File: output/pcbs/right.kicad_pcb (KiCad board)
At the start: 2 copper layers, 137 x 129 mm, 79 parts

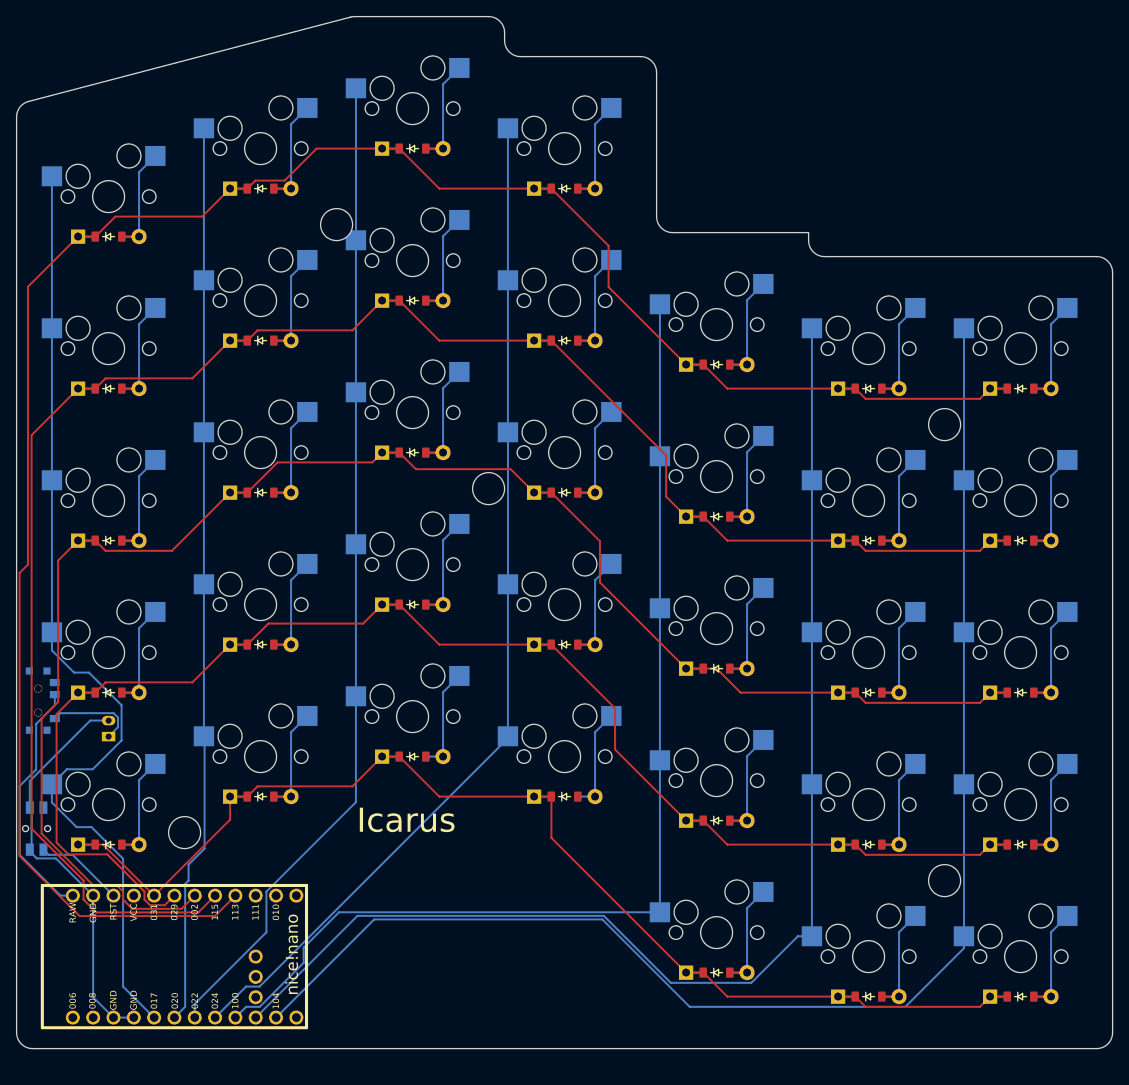
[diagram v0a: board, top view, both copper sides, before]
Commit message: redesign for short board, left but no right pcb. Final pcbs for old design
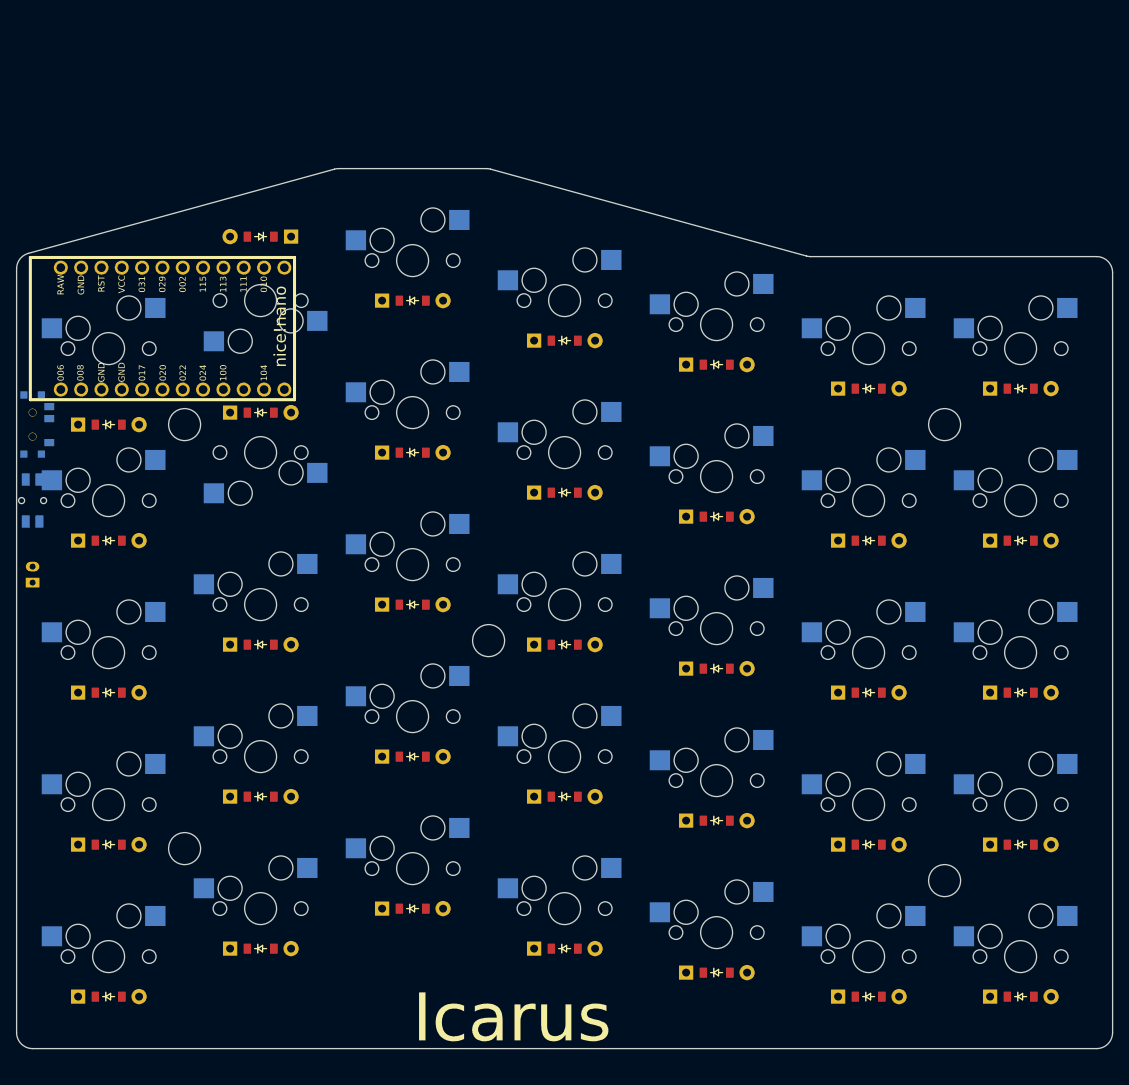
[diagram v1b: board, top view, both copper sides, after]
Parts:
- removed the ? at (261.5, 184.5)
- removed the ? at (299.5, 141.5)
- removed the ? at (280.5, 108.5)
- added ?: , HOLE_M2_TH, F.Cu at (299.5, 160.5)
- added ?: , HOLE_M2_TH, F.Cu at (261.5, 133.5)
- added ?: , HOLE_M2_TH, F.Cu at (261.5, 186.5)
- moved D29 84.2 mm to (252.0, 205.0)
- moved D30 84.2 mm to (252.0, 186.0)
- moved S29 84.2 mm to (252.0, 200.0)
- moved S30 84.2 mm to (252.0, 181.0)
- moved MCU1 78.5 mm to (260.0, 121.5)
- moved B1 41.0 mm to (242.5, 143.0)
- moved T1 34.5 mm to (242.5, 133.5)
- moved D34 26.9 mm to (271.0, 110.0), turned to -180 degrees
- moved D33 24.8 mm to (271.0, 132.0)
- moved D35 23.5 mm to (252.0, 133.5)
- moved S34 23.0 mm to (271.0, 137.0), turned to 180 degrees
- moved S35 23.0 mm to (271.0, 118.0), turned to 180 degrees
- moved JST1 21.5 mm to (242.5, 152.2)
- moved D16 19.0 mm to (309.0, 199.0)
- moved D17 19.0 mm to (309.0, 180.0)
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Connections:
- D1 pad 1: P031 -> P029
- D10 pad 1: P113 -> P031
- D11 pad 1: P031 -> P029
- D12 pad 1: P029 -> P002
- D13 pad 1: P002 -> P115
- D14 pad 1: P115 -> P113
- D15 pad 1: P113 -> P031
- D16 pad 1: P031 -> P029
- D17 pad 1: P029 -> P002
- D18 pad 1: P002 -> P115
- D19 pad 1: P115 -> P113
- D2 pad 1: P029 -> P002
- D20 pad 1: P113 -> P031
- D21 pad 1: P031 -> P029
- D22 pad 1: P029 -> P002
- D23 pad 1: P002 -> P115
- D24 pad 1: P115 -> P113
- D25 pad 1: P113 -> P031
- D26 pad 1: P031 -> P029
- D27 pad 1: P029 -> P002
- D28 pad 1: P002 -> P115
- D29 pad 1: P115 -> P029
- D29 pad 2: mirror_index_top -> mirror_inner_space
- D3 pad 1: P002 -> P115
- D30 pad 1: P113 -> P002
- D30 pad 2: mirror_index_num -> mirror_inner_bottom
- D31 pad 1: P031 -> P115
- D31 pad 2: mirror_inner_space -> mirror_inner_home
- D32 pad 1: P029 -> P113
- D32 pad 2: mirror_inner_bottom -> mirror_inner_top
- D33 pad 1: P002 -> P113
- D33 pad 2: mirror_inner_home -> mirror_index_top
- D34 pad 1: P115 -> P031
- D34 pad 2: mirror_inner_top -> mirror_index_num
- D35 pad 1: P113 -> P031
- D4 pad 1: P115 -> P113
- D5 pad 1: P113 -> P031
- D6 pad 1: P031 -> P029
- D7 pad 1: P029 -> P002
- D8 pad 1: P002 -> P115
- D9 pad 1: P115 -> P113
- S1 pad 1: P104 -> P024
- S10 pad 1: P011 -> P100
- S11 pad 1: P100 -> P011
- S12 pad 1: P100 -> P011
- S13 pad 1: P100 -> P011
- S14 pad 1: P100 -> P011
- S15 pad 1: P100 -> P011
- S16 pad 1: P024 -> P104
- S17 pad 1: P024 -> P104
- S18 pad 1: P024 -> P104
- S19 pad 1: P024 -> P104
- S2 pad 1: P104 -> P024
- S20 pad 1: P024 -> P104
- S21 pad 1: P022 -> P106
- S22 pad 1: P022 -> P106
- S23 pad 1: P022 -> P106
- S24 pad 1: P022 -> P106
- S25 pad 1: P022 -> P106
- S29 pad 1: P020 -> P017
- S29 pad 2: mirror_index_top -> mirror_inner_space
- S3 pad 1: P104 -> P024
- S30 pad 1: P020 -> P017
- S30 pad 2: mirror_index_num -> mirror_inner_bottom
- S31 pad 2: mirror_inner_space -> mirror_inner_home
- S32 pad 2: mirror_inner_bottom -> mirror_inner_top
- S33 pad 2: mirror_inner_home -> mirror_inner_num
- S34 pad 1: P017 -> P020
- S34 pad 2: mirror_inner_top -> mirror_index_top
- S35 pad 1: P017 -> P020
- S35 pad 2: mirror_inner_num -> mirror_index_num
- S4 pad 1: P104 -> P024
- S5 pad 1: P104 -> P024
- S6 pad 1: P011 -> P100
- S7 pad 1: P011 -> P100
- S8 pad 1: P011 -> P100
- S9 pad 1: P011 -> P100
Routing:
- net P113: track 263.9 -> 0.00 mm
- net P115: track 239.3 -> 0.00 mm
- net P002: track 216.2 -> 0.00 mm
- net P029: track 191.3 -> 0.00 mm
- net P104: track 176.1 -> 0.00 mm
- net P031: track 159.3 -> 0.00 mm
- net P011: track 156.7 -> 0.00 mm
- net P100: track 135.6 -> 0.00 mm
- net P024: track 127.3 -> 0.00 mm
- net P022: track 124.5 -> 0.00 mm
- net P017: track 121.7 -> 0.00 mm
- net P020: track 112.8 -> 0.00 mm
- net GND: track 51.0 -> 0.00 mm
- net RAW: track 30.6 -> 0.00 mm
- net mirror_ring_home: track 15.2 -> 0.00 mm
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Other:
- board size 137 x 129 mm -> 137 x 110 mm
- net class Default added: clearance 0.2, trace_width 0.25, via_dia 0.8, via_drill 0.4
